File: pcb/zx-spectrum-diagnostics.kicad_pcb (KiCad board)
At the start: 2 copper layers, 99.9 x 98.2 mm, 74 parts, among them J101 Conn_01x04, J201 Conn_01x20_Female, J202 Conn_01x20_Female, J203 Conn_01x20_Female, Q101 PMBT2222A, SW101 SW_SPST, U101 Pico, U102 Pico

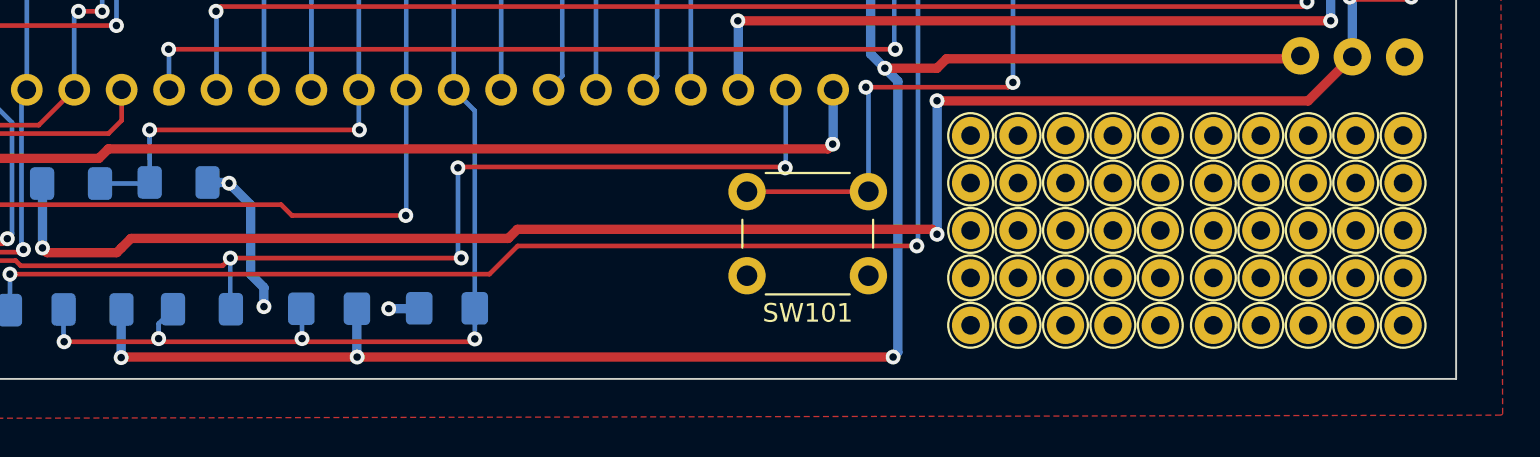
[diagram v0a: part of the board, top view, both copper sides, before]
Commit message: remove test points from v1.2, replace with GND area for clip. updated gerbers, sent for fabrication
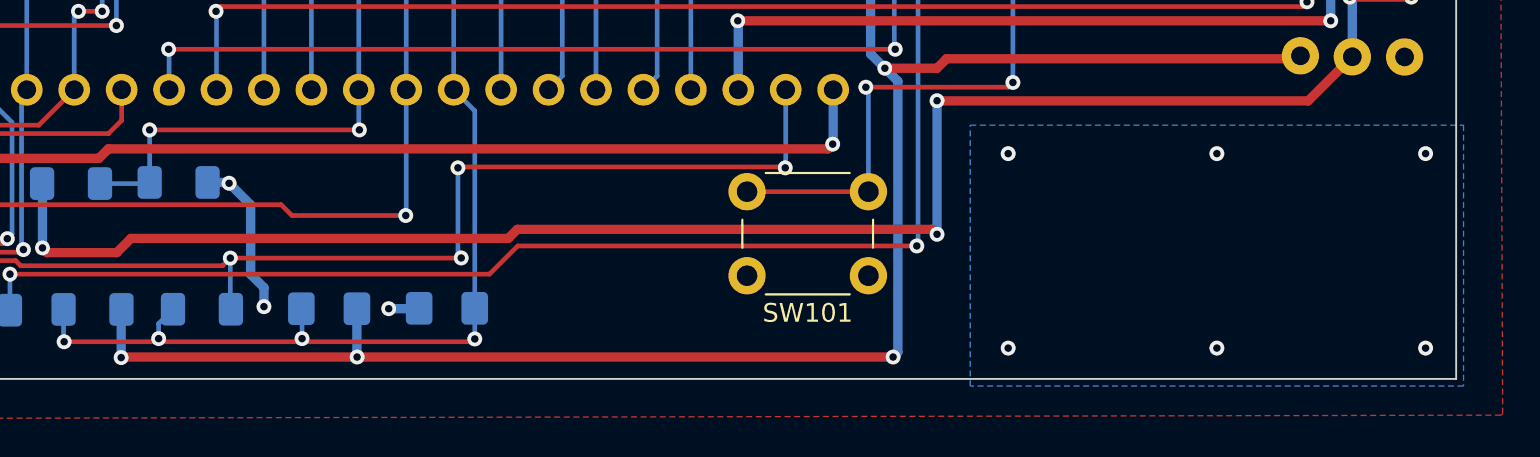
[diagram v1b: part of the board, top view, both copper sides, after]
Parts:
- removed REF** (x2), REF**1 (x2), REF**10 (x2), REF**11 (x2), REF**12 (x2), REF**13 (x2), REF**14 (x2), REF**15 (x2), REF**16 (x2), REF**17 (x2), REF**18 (x2), REF**19 (x2), REF**2 (x2), REF**20 (x2), REF**21 (x2), REF**22 (x2), REF**23 (x2), REF**24 (x2), REF**3 (x2), REF**4 (x2), REF**5 (x2), REF**6 (x2), REF**7 (x2), REF**8 (x2), REF**9 (x2): TestPoint_THTPad_D2.0mm_Drill1.0mm, TestPoint:TestPoint_THTPad_D2.0mm_Drill1.0mm
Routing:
- net GND: vias 8 -> 14
- added copper zone on B.Cu, net GND
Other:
- board text removed: "Some 3216 footprints with tracks coming from them might be more useful than all these test points? If I want to mount SMD diodes or something?"

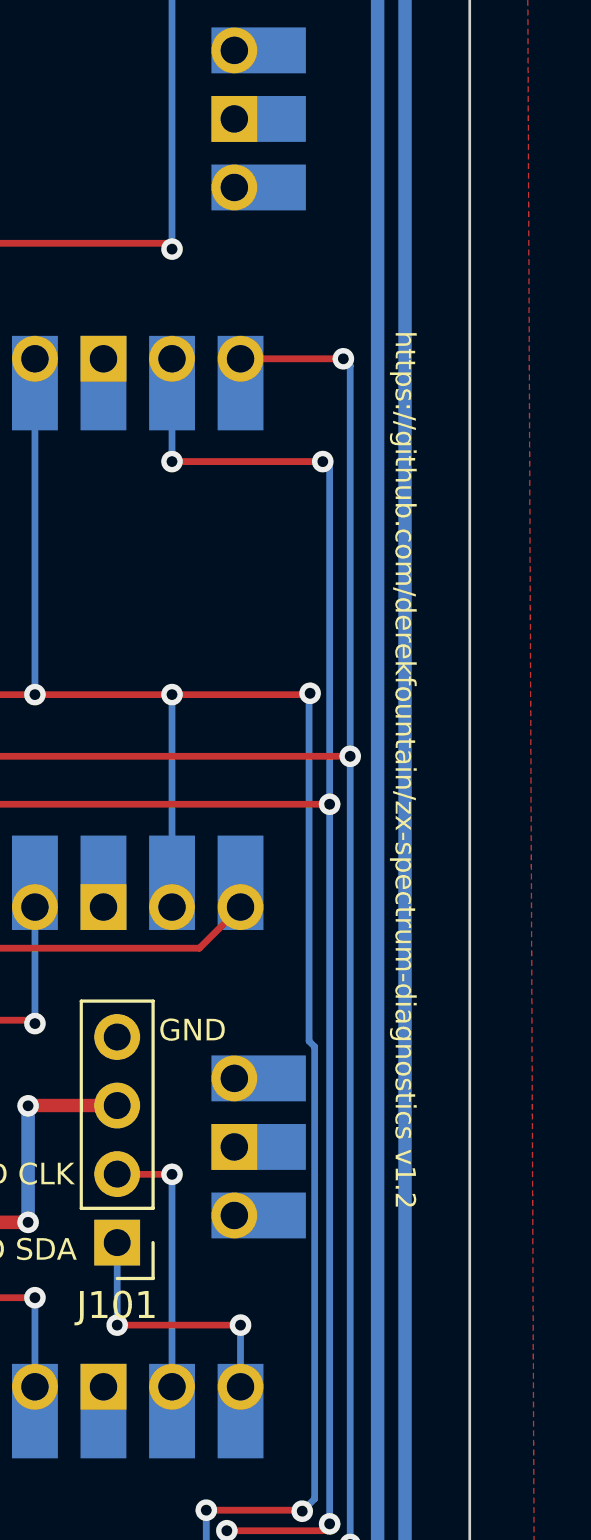
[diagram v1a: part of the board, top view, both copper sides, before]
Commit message: minor updates to labels on silkscreen
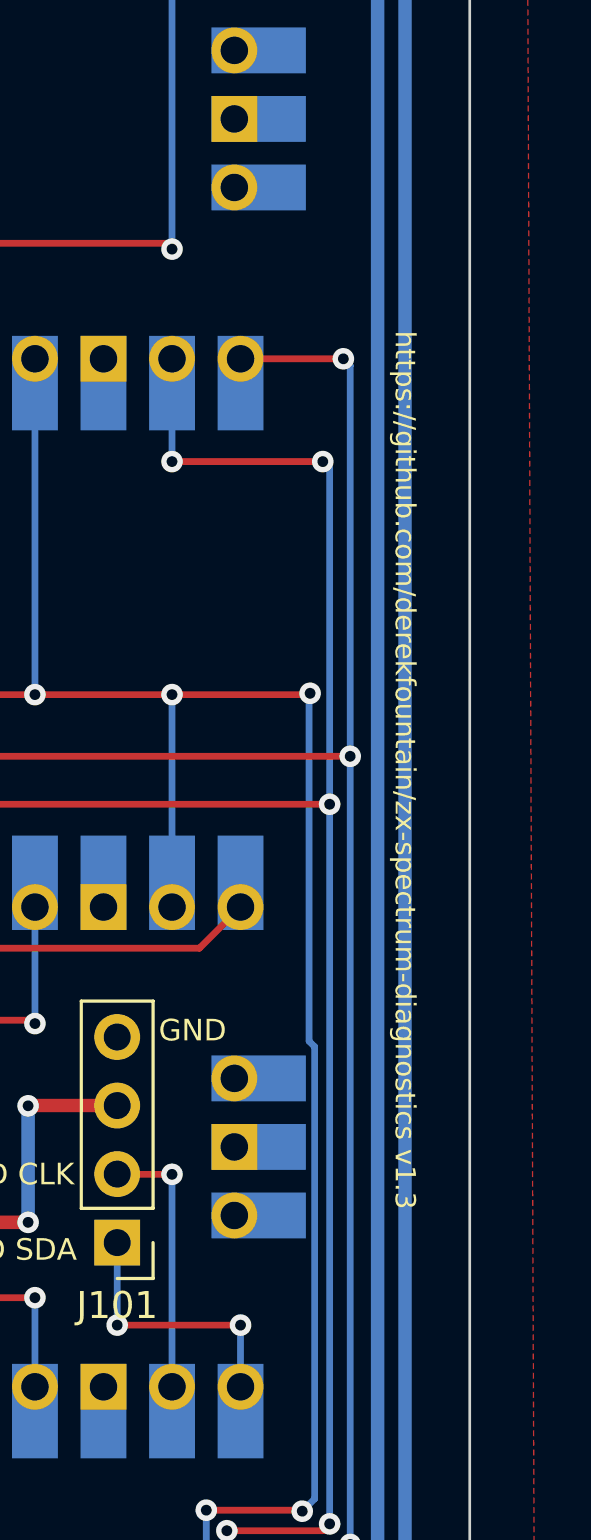
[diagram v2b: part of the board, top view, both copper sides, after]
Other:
- board text added: "https://github.com/derekfountain/zx-spectrum-diagnostics v1.3"
- board text removed: "P2_G16"
- board text removed: "P2_G17"
- board text removed: "P2_G18"
- board text removed: "https://github.com/derekfountain/zx-spectrum-diagnostics v1.2"
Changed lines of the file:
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@@
     (effects (font (size 0.8 0.8) (thickness 0.125)) (justify right mirror))
   )
-  (gr_text "P2_G18" (at 112.88 136.57 30) (layer "B.SilkS")
+  (gr_text "CLK" (at 112.88 136.57 30) (layer "B.SilkS")
     (effects (font (size 0.8 0.8) (thickness 0.125)) (justify right mirror))
   )
@@
   (gr_text "HALT" (at 95.826 111.78 330) (layer "B.SilkS")
     (effects (font (size 0.8 0.8) (thickness 0.125)) (justify right mirror))
-  )
-  (gr_text "P2\nBLIP" (at 125.984 141.224) (layer "B.SilkS")
-    (effects (font (size 0.8 0.8) (thickness 0.125)) (justify mirror))
   )
   (gr_text "A12" (at 89.078 84.04 330) (layer "B.SilkS")
@@
     (effects (font (size 0.8 0.8) (thickness 0.125)) (justify right mirror))
   )
-  (gr_text "P2_G17" (at 110.26 136.66 30) (layer "B.SilkS")
+  (gr_text "RD" (at 110.26 136.66 30) (layer "B.SilkS")
     (effects (font (size 0.8 0.8) (thickness 0.125)) (justify right mirror))
   )
@@
     (effects (font (size 0.8 0.8) (thickness 0.125)) (justify right mirror))
   )
-  (gr_text "P2_G16" (at 107.7 136.64 30) (layer "B.SilkS")
+  (gr_text "MREQ" (at 107.7 136.64 30) (layer "B.SilkS")
     (effects (font (size 0.8 0.8) (thickness 0.125)) (justify right mirror))
   )
@@
   (gr_text "+5V" (at 89.118 86.51 330) (layer "B.SilkS")
     (effects (font (size 0.8 0.8) (thickness 0.125)) (justify right mirror))
-  )
-  (gr_text "P1\nBLIP" (at 123.444 141.224) (layer "B.SilkS")
-    (effects (font (size 0.8 0.8) (thickness 0.125)) (justify mirror))
   )
   (gr_text "GND" (at 171.892 134.844) (layer "B.SilkS")
@@
     (effects (font (size 0.8 0.8) (thickness 0.15)))
   )
-  (gr_text "https://github.com/derekfountain/zx-spectrum-diagnostics v1.2" (at 172.212 101.092 270) (layer "F.SilkS")
+  (gr_text "https://github.com/derekfountain/zx-spectrum-diagnostics v1.3" (at 172.212 101.092 270) (layer "F.SilkS")
     (effects (font (size 0.75 0.75) (thickness 0.15)))
   )
